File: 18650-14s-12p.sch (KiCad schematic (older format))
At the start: 87 parts, among them J1 Conn_01x14, J2 Conn_01x07

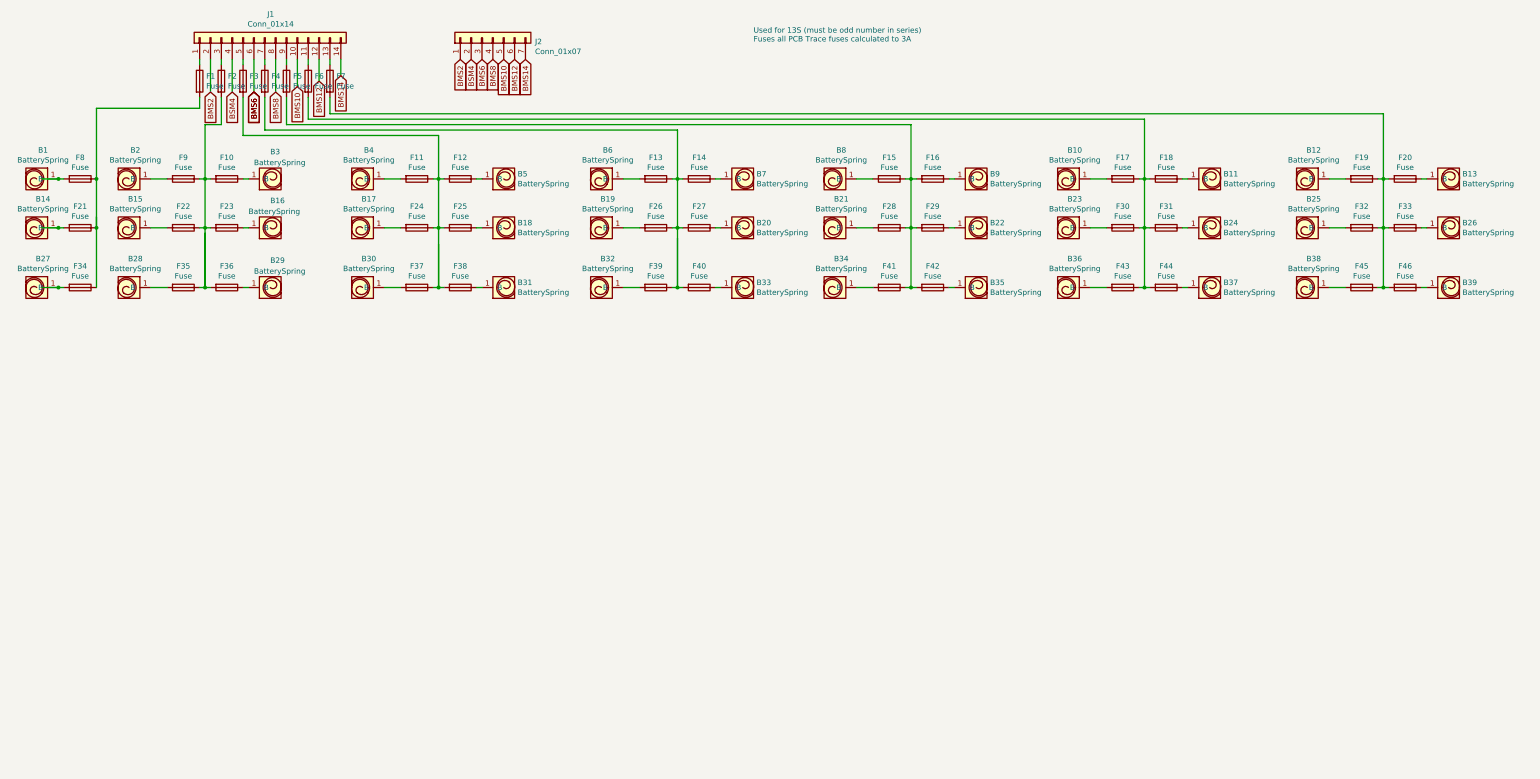
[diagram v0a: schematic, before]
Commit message: Updated to 13s-12p
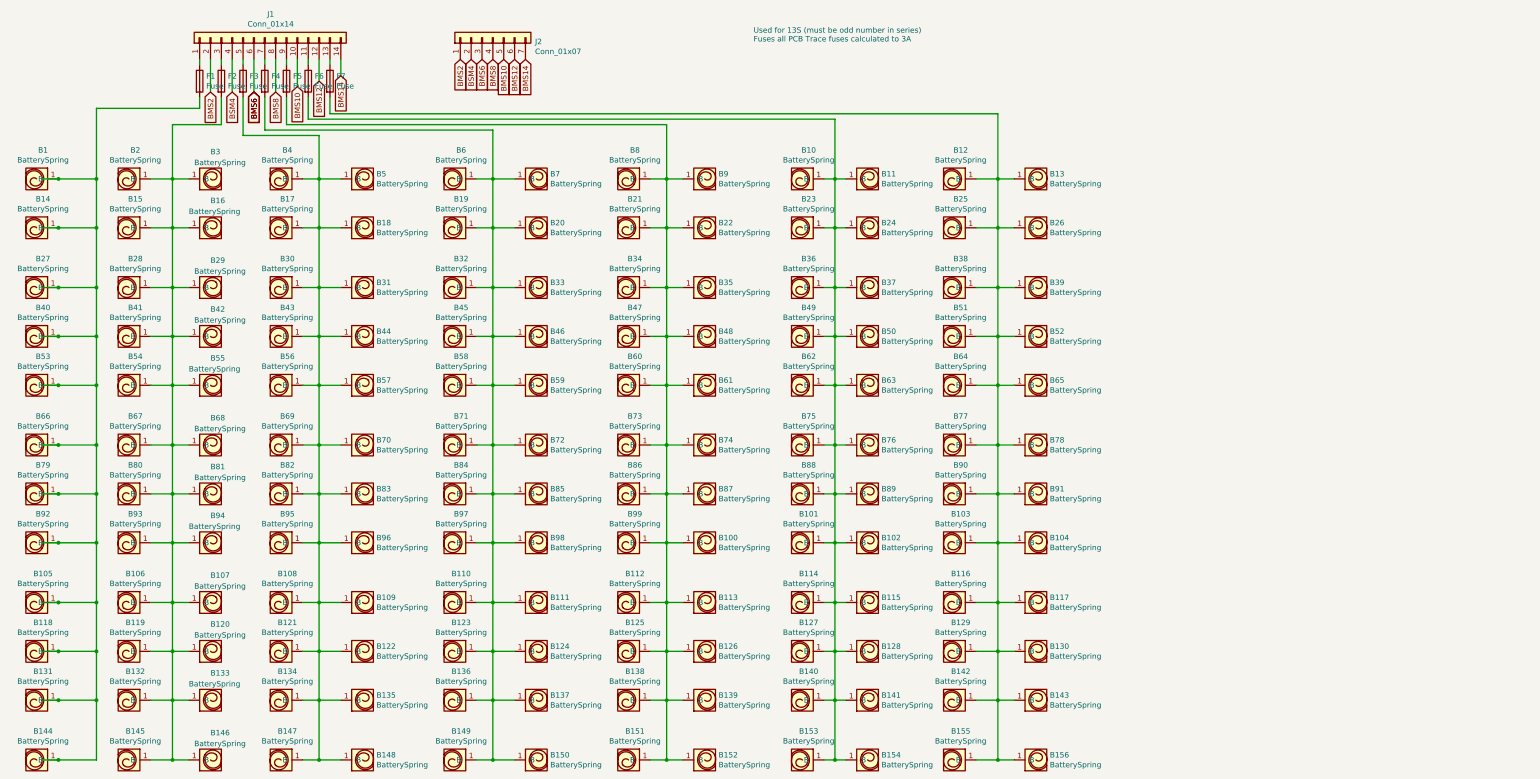
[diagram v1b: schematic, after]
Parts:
- removed F10, F11, F12, F13, F14, F15, F16, F17, F18, F19, F20, F21, F22, F23, F24, F25, F26, F27, F28, F29, F30, F31, F32, F33, F34, F35, F36, F37, F38, F39, F40, F41, F42, F43, F44, F45, F46, F8, F9: Fuse, Fuse:pcbfuse_4a, symbol Device:Fuse
- added B100, B101, B102, B103, B104, B105, B106, B107, B108, B109, B110, B111, B112, B113, B114, B115, B116, B117, B118, B119, B120, B121, B122, B123, B124, B125, B126, B127, B128, B129, B130, B131, B132, B133, B134, B135, B136, B137, B138, B139, B140, B141, B142, B143, B144, B145, B146, B147, B148, B149, B150, B151, B152, B153, B154, B155, B156, B40, B41, B42, B43, B44, B45, B46, B47, B48, B49, B50, B51, B52, B53, B54, B55, B56, B57, B58, B59, B60, B61, B62, B63, B64, B65, B66, B67, B68, B69, B70, B71, B72, B73, B74, B75, B76, B77, B78, B79, B80, B81, B82, B83, B84, B85, B86, B87, B88, B89, B90, B91, B92, B93, B94, B95, B96, B97, B98, B99: BatterySpring, Battery:batteryspring, symbol Mechanical:BatterySpring
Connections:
- wire segments 131 -> 280
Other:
- moved on the sheet: B10, B11, B12, B13, B16, B17, B18, B19, B20, B21, B22, B23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
